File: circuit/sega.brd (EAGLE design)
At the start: 100.6 x 99 mm, 63 parts, among them P1:A|B WIREPAD2,54/1,0, P1:C1 100nF, P1:D WIREPAD2,54/1,0, P1:GND WIREPAD2,54/1,0, P1:G|L WIREPAD2,54/1,0, P1:G|R WIREPAD2,54/1,0, P1:MUX 74LS157N, P1:OK1 PC847, P1:OK2 PC847, P1:R1 10k, P1:R10 750, P1:R11 750, P1:R12 750, P1:R13 750, P1:R14 750, P1:R15 750, P1:R16 750, P1:R2 10k, P1:R3 10k, P1:R4 10k, P1:R5 10k, P1:R6 10k, P1:R7 10k, P1:R8 10k, P1:R9 750, P1:SEL WIREPAD2,54/1,0, P1:S|C WIREPAD2,54/1,0, P1:U WIREPAD2,54/1,0, P1:VCC WIREPAD2,54/1,0, P2:A|B WIREPAD2,54/1,0, P2:C1 100nF, P2:D WIREPAD2,54/1,0, P2:GND WIREPAD2,54/1,0, P2:G|L WIREPAD2,54/1,0, P2:G|R WIREPAD2,54/1,0, P2:MUX 74LS157N, P2:OK1 PC847, P2:OK2 PC847, P2:R1 10k, P2:R10 750, P2:R11 750, P2:R12 750, P2:R13 750, P2:R14 750, P2:R15 750, P2:R16 750, P2:R2 10k, P2:R3 10k, P2:R4 10k, P2:R5 10k, P2:R6 10k, P2:R7 10k, P2:R8 10k, P2:R9 750, P2:SEL WIREPAD2,54/1,0, P2:S|C WIREPAD2,54/1,0, P2:U WIREPAD2,54/1,0, P2:VCC WIREPAD2,54/1,0

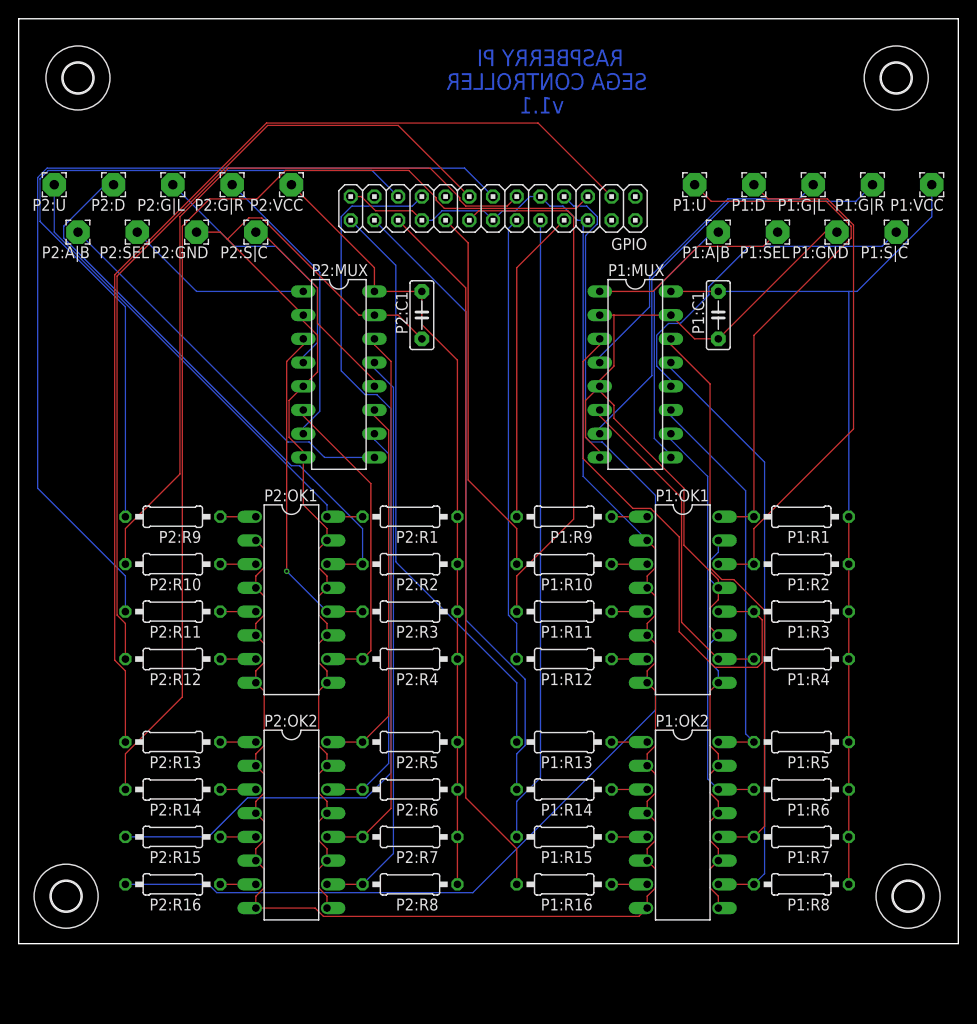
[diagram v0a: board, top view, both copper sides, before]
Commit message: Update circuit design to v1.2
 - Raspberry Pi Zero mounted directly to the board replaces header
 - DB9 connectors replace individual jumper wires to the controller
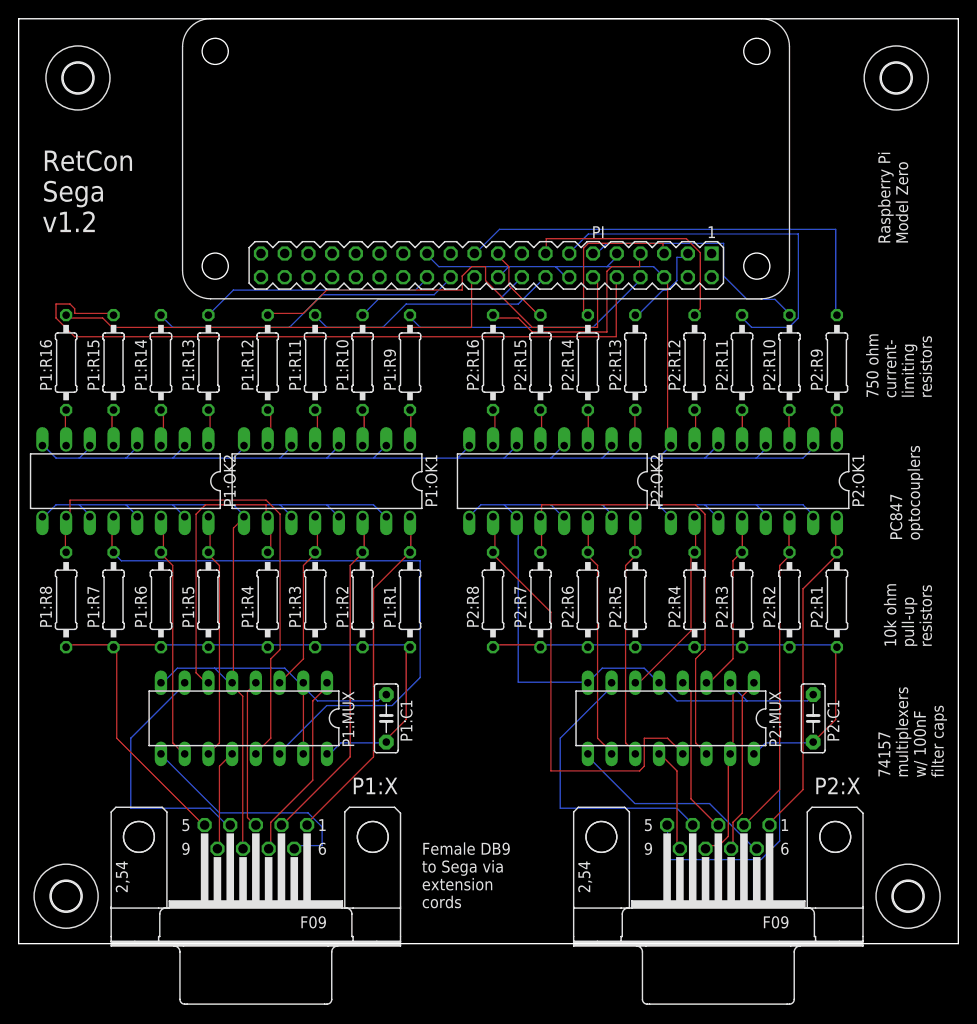
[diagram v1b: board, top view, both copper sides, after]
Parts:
- removed GPIO: (no value), pinhead:2X13
- removed P1:A|B, P1:D, P1:GND, P1:G|L, P1:G|R, P1:SEL, P1:S|C, P1:U, P1:VCC, P2:A|B, P2:D, P2:GND, P2:G|L, P2:G|R, P2:SEL, P2:S|C, P2:U, P2:VCC: WIREPAD2,54/1,0, wirepad:2,54/1,0
- added P1:X, P2:X: (no value), con-subd:F09H
- added PI: PIZERO_THROUGH_HOLE, pizero:PIZERO_THOUGH_HOLE
- moved P1:R8 84.4 mm to (5.08, 36.8), turned to 90 degrees
- moved P1:R7 77.9 mm to (10.2, 36.8), turned to 90 degrees
- moved P1:R16 77.3 mm to (5.08, 62.2), turned to 90 degrees
- moved P2:R9 73.0 mm to (87.6, 62.2), turned to 90 degrees
- moved P1:R6 71.5 mm to (15.2, 36.8), turned to 90 degrees
- moved P1:OK2 70.1 mm to (11.4, 49.5), turned to 180 degrees
- moved P1:R15 70.1 mm to (10.2, 62.2), turned to 90 degrees
- moved P2:R10 69.5 mm to (82.5, 62.2), turned to 90 degrees
- moved P2:R11 66.5 mm to (77.5, 62.2), turned to 90 degrees
- moved P2:R16 65.6 mm to (50.8, 62.2), turned to 90 degrees
- moved P1:R5 65.3 mm to (20.3, 36.8), turned to 90 degrees
- moved P2:R15 64.3 mm to (55.9, 62.2), turned to 90 degrees
- moved P2:R12 64.3 mm to (72.4, 62.2), turned to 90 degrees
- moved P2:R13 64.1 mm to (66.0, 62.2), turned to 90 degrees
- moved P2:R14 63.8 mm to (61.0, 62.2), turned to 90 degrees
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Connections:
- net N$1: now also PI.11; no longer GPIO.11
- net N$10: now also PI.8; no longer GPIO.8
- net N$11: now also PI.10; no longer GPIO.10
- net N$12: now also PI.12; no longer GPIO.12
- net N$13: now also PI.16; no longer GPIO.16
- net N$14: now also PI.18; no longer GPIO.18
- net N$15: now also PI.22; no longer GPIO.22
- net N$16: now also PI.24; no longer GPIO.24
- net N$17: now also PI.26; no longer GPIO.26
- net N$2: now also PI.14, PI.20, PI.25, PI.6, PI.9; no longer GPIO.14, GPIO.20, GPIO.25, GPIO.6, GPIO.9
- net N$3: now also PI.13; no longer GPIO.13
- net N$4: now also PI.3; no longer GPIO.3
- net N$5: now also PI.5; no longer GPIO.5
- net N$6: now also PI.7; no longer GPIO.7
- net N$7: now also PI.15; no longer GPIO.15
- net N$8: now also PI.19; no longer GPIO.19
- net N$9: now also PI.21; no longer GPIO.21
- net P1:A|B: now also P1:X.6; no longer P1:A|B.1
- net P1:D: now also P1:X.2; no longer P1:D.1
- net P1:GND: now also P1:X.8; no longer P1:GND.1
- net P1:G|L: now also P1:X.3; no longer P1:G|L.1
- net P1:G|R: now also P1:X.4; no longer P1:G|R.1
- net P1:SEL: now also P1:X.7; no longer P1:SEL.1
- net P1:S|C: now also P1:X.9; no longer P1:S|C.1
- net P1:U: now also P1:X.1; no longer P1:U.1
- net P1:VCC: now also P1:X.5; no longer P1:VCC.1
- net P2:A|B: now also P2:X.6; no longer P2:A|B.1
- net P2:D: now also P2:X.2; no longer P2:D.1
- net P2:GND: now also P2:X.8; no longer P2:GND.1
- net P2:G|L: now also P2:X.3; no longer P2:G|L.1
- net P2:G|R: now also P2:X.4; no longer P2:G|R.1
- net P2:SEL: now also P2:X.7; no longer P2:SEL.1
- net P2:S|C: now also P2:X.9; no longer P2:S|C.1
- net P2:U: now also P2:X.1; no longer P2:U.1
- net P2:VCC: now also P2:X.5; no longer P2:VCC.1
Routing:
- net N$4: track 113.7 -> 9.89 mm
- net N$6: track 126.9 -> 24.6 mm
- net N$8: track 103.3 -> 8.52 mm
- net N$5: track 111.1 -> 17.4 mm
- net N$7: track 88.9 -> 25.7 mm
- net N$3: track 100.8 -> 41.6 mm
- net N$1: track 80.1 -> 26.8 mm
- net N$2: track 198.2 -> 159.9 mm
- net P1:L: track 57.8 -> 19.6 mm
- net N$17: track 63.2 -> 25.1 mm
- net N$16: track 68.0 -> 33.8 mm
- net N$9: track 79.9 -> 49.0 mm
- net N$13: track 56.7 -> 27.5 mm
- net N$15: track 76.4 -> 49.4 mm
- net P1:S|C: track 36.8 -> 10.8 mm
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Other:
- board text added: "10k ohm pull-up resistors"
- board text added: "74157 multiplexers w/ 100nF filter caps"
- board text added: "750 ohm current- limiting resistors"
- board text added: "Female DB9 to Sega via extension cords"
- board text added: "PC847 optocouplers"
- board text added: "Raspberry Pi Model Zero"
- board text added: "RetCon Sega v1.2"
- board text removed: "RASPBERRY PI"
- board text removed: "SEGA CONTROLLER"
- board text removed: "v1.1"

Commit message: Add missing pull-up resistor to circuit
A pull-up was missing on the select pin.
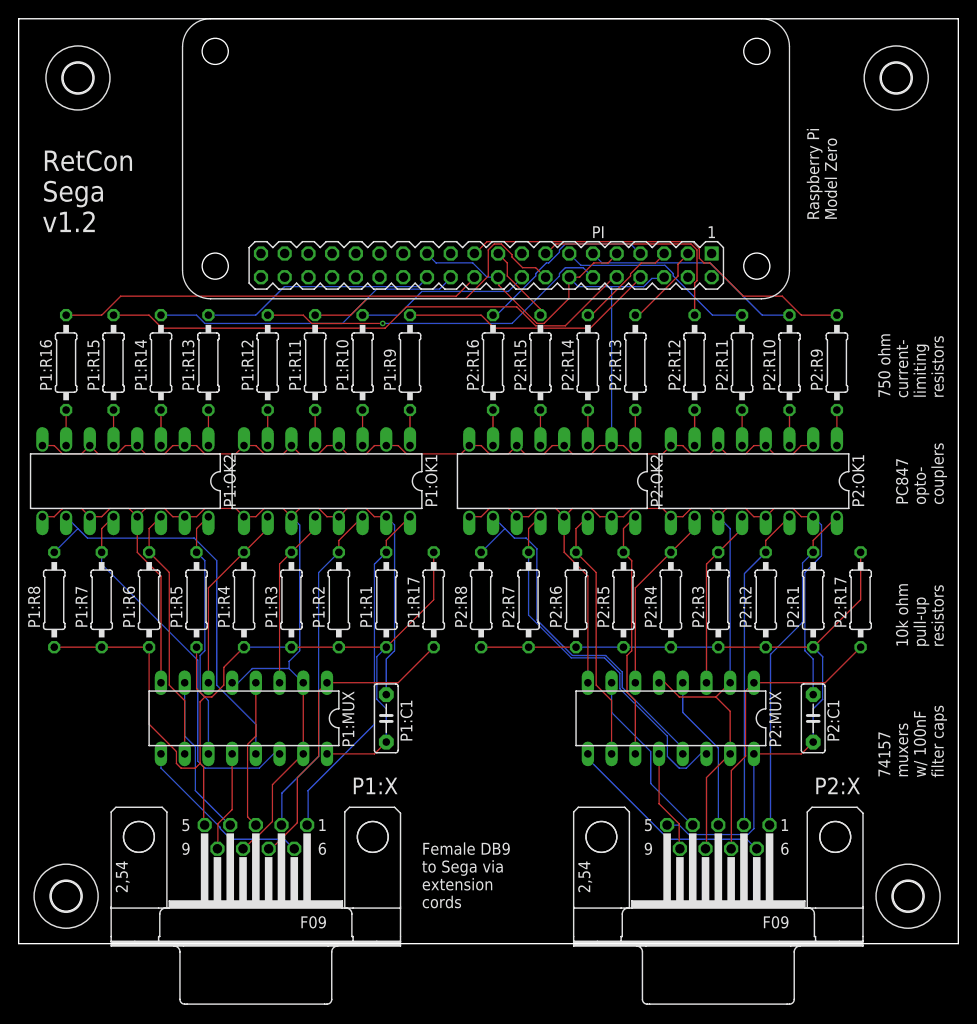
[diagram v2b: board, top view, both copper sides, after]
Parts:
- added P1:R17, P2:R17: 10k, resistor:0207/10
- moved P2:R4 2.54 mm to (69.8, 36.8)
- moved P1:R4 2.54 mm to (24.1, 36.8)
- moved P1:R1 2.54 mm to (39.4, 36.8)
- moved P1:R2 2.54 mm to (34.3, 36.8)
- moved P1:R3 2.54 mm to (29.2, 36.8)
- moved P2:R1 2.54 mm to (85.1, 36.8)
- moved P2:R2 2.54 mm to (80.0, 36.8)
- moved P2:R3 2.54 mm to (74.9, 36.8)
- moved P2:R5 1.27 mm to (64.8, 36.8)
- moved P2:R6 1.27 mm to (59.7, 36.8)
- moved P2:R7 1.27 mm to (54.6, 36.8)
- moved P1:R8 1.27 mm to (3.81, 36.8)
- moved P1:R5 1.27 mm to (19.1, 36.8)
- moved P1:R6 1.27 mm to (14.0, 36.8)
- moved P1:R7 1.27 mm to (8.89, 36.8)
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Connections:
- net P1:SEL: now also P1:R17.1
- net P1:VCC: now also P1:R17.2
- net P2:SEL: now also P2:R17.1
- net P2:VCC: now also P2:R17.2
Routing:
- net P1:S: track 68.2 -> 40.7 mm
- net N$3: track 41.6 -> 21.4 mm
- net P1:VCC: track 79.5 -> 99.6 mm
- net N$11: track 75.7 -> 58.4 mm
- net P1:SEL: track 20.3 -> 33.5 mm
- net P2:SEL: track 18.7 -> 31.8 mm
- net P2:G|R: track 30.7 -> 18.9 mm
- net P1:R: track 32.2 -> 20.4 mm
- net P1:C: track 55.7 -> 44.1 mm
- net P1:G|R: track 27.3 -> 17.3 mm
- net P2:S: track 49.7 -> 39.8 mm
- net N$2: track 159.9 -> 150.0 mm
- net N$12: track 47.5 -> 38.3 mm, vias 0 -> 1
- net P2:C: track 48.0 -> 40.2 mm
- net N$5: track 17.4 -> 11.1 mm
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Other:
- board text added: "74157 muxers w/ 100nF filter caps"
- board text added: "PC847 opto- couplers"
- board text removed: "74157 multiplexers w/ 100nF filter caps"
- board text removed: "PC847 optocouplers"
